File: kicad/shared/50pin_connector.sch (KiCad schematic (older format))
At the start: 1 part, among them P5 CONN_02X25

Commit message: connector
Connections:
- net /CS_RES02: now reaches P5.20 (P20)
- net /OE2: now reaches P5.37 (P37)
- net /WE2: now reaches P5.38 (P38)
- no-connect marks 0 -> 16

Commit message: connector
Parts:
- P5: footprint (none) -> Pin_Headers:Pin_Header_Angled_2x25
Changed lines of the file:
@@
 F 0 "P5" H 5550 5050 50  0000 C CNN
 F 1 "CONN_02X25" V 5550 3750 50  0000 C CNN
-F 2 "" H 5550 3000 60  0000 C CNN
+F 2 "Pin_Headers:Pin_Header_Angled_2x25" H 5550 3000 60  0001 C CNN
 F 3 "" H 5550 3000 60  0000 C CNN
 	1    5550 3750
@@
 Text Label 4850 2700 0    60   ~ 0
 D
-Text Label 4550 3750 0    60   ~ 0
+Text Label 4350 3750 0    60   ~ 0
 A[0..15]
-Text Label 6450 3650 0    60   ~ 0
-A
 Text GLabel 5250 4350 0    60   Input ~ 0
 /OE2
@@
 Text GLabel 5850 3450 2    60   Input ~ 0
 /CS_RES02
-Text HLabel 6650 3950 2    60   Input ~ 0
+Text HLabel 3550 4900 2    60   Input ~ 0
 A0
 Entry Wire Line
-	6450 3850 6550 3950
-Wire Wire Line
-	6550 3950 6650 3950
-Text HLabel 6650 3850 2    60   Input ~ 0
+	3350 4800 3450 4900
+Text HLabel 3550 4700 2    60   Input ~ 0
 A2
-Text HLabel 6650 3750 2    60   Input ~ 0
+Text HLabel 3550 4500 2    60   Input ~ 0
 A4
 Entry Wire Line
-	6450 3750 6550 3850
-Entry Wire Line
-	6450 3650 6550 3750
-Wire Wire Line
-	6550 3750 6650 3750
-Wire Wire Line
-	6650 3850 6550 3850
-Entry Wire Line
-	4550 3850 4650 3750
-Text HLabel 4550 3850 0    60   Input ~ 0
+	3350 4500 3450 4600
+Entry Wire Line
+	3350 4400 3450 4500
+Wire Wire Line
+	3450 4500 3550 4500
+Entry Wire Line
+	3450 4700 3350 4600
+Text HLabel 3550 4600 2    60   Input ~ 0
 A3
 Entry Wire Line
-	4550 3950 4650 3850
-Text HLabel 4550 3950 0    60   Input ~ 0
+	3450 4800 3350 4700
+Text HLabel 3550 4800 2    60   Input ~ 0
 A1
+Wire Bus Line
+	3350 4100 3350 4950
+Text Label 3350 4150 0    60   ~ 0
+A[0..15]
+Wire Wire Line
+	3450 4900 3550 4900
+Wire Wire Line
+	3450 4800 3550 4800
+Wire Wire Line
+	3450 4600 3550 4600
+Wire Wire Line
+	3550 4700 3450 4700
+Wire Bus Line
+	3350 2700 3350 3750
+Entry Wire Line
+	3350 3050 3450 3150
+Entry Wire Line
+	3350 3250 3450 3350
+Entry Wire Line
+	3350 3450 3450 3550
+Entry Wire Line
+	3350 3650 3450 3750
+Wire Wire Line
+	3450 3150 3600 3150
+Wire Wire Line
+	3450 3350 3600 3350
+Wire Wire Line
+	3450 3550 3600 3550
+Wire Wire Line
+	3450 3750 3600 3750
+Text Label 3450 3150 0    60   ~ 0
+D7
+Text Label 3450 3350 0    60   ~ 0
+D5
+Text Label 3450 3550 0    60   ~ 0
+D3
+Text Label 3450 3750 0    60   ~ 0
+D1
+Text Label 3350 2650 0    60   ~ 0
+D[0..7]
+Entry Wire Line
+	3450 3250 3350 3150
+Entry Wire Line
+	3450 3450 3350 3350
+Entry Wire Line
+	3450 3650 3350 3550
+Entry Wire Line
+	3450 3850 3350 3750
+Wire Wire Line
+	3600 3250 3450 3250
+Wire Wire Line
+	3600 3450 3450 3450
+Wire Wire Line
+	3600 3650 3450 3650
+Wire Wire Line
+	3600 3850 3450 3850
+Text Label 3550 3250 2    60   ~ 0
+D6
+Text Label 3550 3450 2    60   ~ 0
+D4
+Text Label 3550 3650 2    60   ~ 0
+D2
+Text Label 3550 3850 2    60   ~ 0
+D0
+Text HLabel 3600 3850 2    60   Input ~ 0
+D0
+Text HLabel 3600 3750 2    60   Input ~ 0
+D1
+Text HLabel 3600 3650 2    60   Input ~ 0
+D2
+Text HLabel 3600 3550 2    60   Input ~ 0
+D3
+Text HLabel 3600 3450 2    60   Input ~ 0
+D4
+Text HLabel 3600 3350 2    60   Input ~ 0
+D5
+Text HLabel 3600 3250 2    60   Input ~ 0
+D6
+Text HLabel 3600 3150 2    60   Input ~ 0
+D7
+Text Label 3450 4900 0    60   ~ 0
+A0
+Text Label 3450 4800 0    60   ~ 0
+A1
+Text Label 3450 4700 0    60   ~ 0
+A2
+Text Label 3450 4600 0    60   ~ 0
+A3
+Text Label 3450 4500 0    60   ~ 0
+A4
 $EndSCHEMATC

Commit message: connector
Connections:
- net /RW: now also P5.15 (P15); no longer P5.16 (P16)
- net D0: now also P5.13 (P13); no longer P5.14 (P14)
- net D1: now also P5.12 (P12); no longer P5.13 (P13)
- net D2: now also P5.11 (P11); no longer P5.12 (P12)
- net D3: now also P5.10 (P10); no longer P5.11 (P11)
- net D4: now also P5.9 (P9); no longer P5.10 (P10)
- net D5: now also P5.8 (P8); no longer P5.9 (P9)
- net D6: now also P5.7 (P7); no longer P5.8 (P8)
- net D7: now also P5.6 (P6); no longer P5.7 (P7)
- net GND: now also P5.47 (P47), P5.48 (P48), P5.49 (P49), P5.50 (P50)
- net RDY: now also P5.17 (P17); no longer P5.18 (P18)
- net VCC: now also P5.43 (P43), P5.44 (P44), P5.45 (P45), P5.46 (P46)
- net /CS_IO2: now reaches P5.19 (P19)
- net /ROMOFF: now reaches P5.5 (P5)
- net /CSR_VDP renamed /CS_VDP
- net /CSW_VDP renamed A5
- net /CS_RES02 renamed /CS_IO1
- net /CS_VIA renamed /CS_IO0
- net /OE2: no longer names the net of P5.37 (P37)
- net /WE2: no longer names the net of P5.38 (P38)
- net E_LCD renamed /CS_SND
- no-connect marks 16 -> 10
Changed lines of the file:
@@
 LIBS:contrib
 LIBS:valves
-LIBS:65xxx
-LIBS:gal
-LIBS:UART
-LIBS:osc
-LIBS:steckschwein-cache
 EELAYER 24 0
 EELAYER END
 $Descr A4 11693 8268
 encoding utf-8
-Sheet 2 2
+Sheet 1 1
 Title ""
 Date ""
@@
 /NMI
 Wire Bus Line
-	4850 2700 4850 3050
-Entry Wire Line
-	4850 2750 4950 2850
-Entry Wire Line
-	4850 2850 4950 2950
-Entry Wire Line
-	4850 2950 4950 3050
-Entry Wire Line
-	4850 3050 4950 3150
-Wire Wire Line
-	4950 2850 5300 2850
-Wire Wire Line
-	4950 2950 5300 2950
-Wire Wire Line
-	4950 3050 5300 3050
-Wire Wire Line
-	4950 3150 5300 3150
-Text Label 4950 2850 0    60   ~ 0
+	6400 2600 6400 2950
+Entry Wire Line
+	6400 2650 6300 2750
+Entry Wire Line
+	6400 2750 6300 2850
+Entry Wire Line
+	6400 2850 6300 2950
+Entry Wire Line
+	6400 2950 6300 3050
+Text Label 6300 2750 2    60   ~ 0
 D7
-Text Label 4950 2950 0    60   ~ 0
+Text Label 6300 2850 2    60   ~ 0
 D5
-Text Label 4950 3050 0    60   ~ 0
+Text Label 6300 2950 2    60   ~ 0
 D3
-Text Label 4950 3150 0    60   ~ 0
+Text Label 6300 3050 2    60   ~ 0
 D1
 Wire Bus Line
-	6300 2700 6300 3050
-Entry Wire Line
-	6200 2850 6300 2750
-Entry Wire Line
-	6200 2950 6300 2850
-Entry Wire Line
-	6200 3050 6300 2950
-Entry Wire Line
-	6200 3150 6300 3050
-Wire Wire Line
-	5800 2850 6200 2850
-Wire Wire Line
-	5800 2950 6200 2950
-Wire Wire Line
-	5800 3050 6200 3050
-Wire Wire Line
-	5800 3150 6200 3150
-Wire Wire Line
-	5800 3250 5850 3250
-Text GLabel 5850 3250 2    60   Input ~ 0
+	4650 2700 4650 3050
+Entry Wire Line
+	4750 2850 4650 2750
+Entry Wire Line
+	4750 2950 4650 2850
+Entry Wire Line
+	4750 3050 4650 2950
+Entry Wire Line
+	4750 3150 4650 3050
+Text GLabel 5250 3250 0    60   Input ~ 0
 /RW
-Text GLabel 5850 3350 2    60   Input ~ 0
+Text GLabel 5250 3350 0    60   Input ~ 0
 RDY
-Wire Wire Line
-	5800 3350 5850 3350
 Wire Wire Line
 	5300 3550 5250 3550
 Text GLabel 5250 3550 0    60   Input ~ 0
-E_LCD
+/CS_SND
 Wire Wire Line
 	5800 3550 5850 3550
 Text GLabel 5850 3550 2    60   Input ~ 0
-/CS_VIA
+/CS_IO0
 Text GLabel 5250 3650 0    60   Input ~ 0
 /CS_UART
@@
 	5300 3650 5250 3650
 Text GLabel 5850 3650 2    60   Input ~ 0
-/CSR_VDP
-Text GLabel 5250 3750 0    60   Input ~ 0
-/CSW_VDP
-Wire Wire Line
-	5250 3750 5300 3750
+/CS_VDP
+Wire Wire Line
+	4750 3750 5300 3750
 Wire Wire Line
 	5800 3650 5850 3650
@@
 	5800 3950 6350 3950
 Wire Bus Line
-	4650 3750 4650 4000
+	4650 3650 4650 4000
 Entry Wire Line
 	4650 3750 4750 3850
@@
 Text GLabel 5850 4150 2    60   Input ~ 0
 /WE
-Text Label 6100 2850 0    60   ~ 0
+Text Label 4850 2850 2    60   ~ 0
 D6
-Text Label 6100 2950 0    60   ~ 0
+Text Label 4850 2950 2    60   ~ 0
 D4
-Text Label 6100 3050 0    60   ~ 0
+Text Label 4850 3050 2    60   ~ 0
 D2
-Text Label 6100 3150 0    60   ~ 0
+Text Label 4850 3150 2    60   ~ 0
 D0
 Text Label 6250 3950 0    60   ~ 0
@@
 Text Label 4750 3850 0    60   ~ 0
 A3
-Text Label 6300 2700 0    60   ~ 0
+Text Label 4850 2700 2    60   ~ 0
 D
-Text Label 4850 2700 0    60   ~ 0
+Text Label 6400 2600 2    60   ~ 0
 D
-Text Label 4350 3750 0    60   ~ 0
+Text Label 4300 3650 0    60   ~ 0
 A[0..15]
-Text GLabel 5250 4350 0    60   Input ~ 0
-/OE2
-Text GLabel 5850 4350 2    60   Input ~ 0
-/WE2
-Wire Wire Line
-	5850 4350 5800 4350
-Wire Wire Line
-	5250 4350 5300 4350
-NoConn ~ 5300 3250
-NoConn ~ 5300 3350
-NoConn ~ 5300 3450
 NoConn ~ 5800 4250
 NoConn ~ 5300 4450
 NoConn ~ 5300 4550
-NoConn ~ 5300 4650
-NoConn ~ 5300 4750
-NoConn ~ 5300 4850
-NoConn ~ 5300 4950
 NoConn ~ 5800 4450
 NoConn ~ 5800 4550
-NoConn ~ 5800 4650
-NoConn ~ 5800 4750
-NoConn ~ 5800 4850
-NoConn ~ 5800 4950
 Wire Wire Line
 	5800 3450 5850 3450
 Text GLabel 5850 3450 2    60   Input ~ 0
-/CS_RES02
+/CS_IO1
 Text HLabel 3550 4900 2    60   Input ~ 0
 A0
@@
 Text Label 3450 4500 0    60   ~ 0
 A4
+Text GLabel 5250 3450 0    60   Input ~ 0
+/CS_IO2
+Wire Wire Line
+	5250 3450 5300 3450
+Wire Wire Line
+	5250 3350 5300 3350
+NoConn ~ 5800 3350
+Wire Wire Line
+	5300 2850 4750 2850
+Wire Wire Line
+	5300 2950 4750 2950
+Wire Wire Line
+	5300 3050 4750 3050
+Wire Wire Line
+	5300 3150 4750 3150
+Wire Wire Line
+	5800 2750 6300 2750
+Wire Wire Line
+	6300 2850 5800 2850
+Wire Wire Line
+	6300 2950 5800 2950
+Wire Wire Line
+	6300 3050 5800 3050
+Text GLabel 5250 2750 0    60   Input ~ 0
+/ROMOFF
+Wire Wire Line
+	5250 2750 5300 2750
+NoConn ~ 5800 3150
+Wire Wire Line
+	5250 3250 5300 3250
+NoConn ~ 5800 3250
+Entry Wire Line
+	4650 3650 4750 3750
+Text Label 4750 3750 0    60   ~ 0
+A5
+NoConn ~ 5800 4350
+NoConn ~ 5300 4350
+$Comp
+L GND #PWR?
+U 1 1 5436D639
+P 5250 5150
+F 0 "#PWR?" H 5250 5150 30  0001 C CNN
+F 1 "GND" H 5250 5080 30  0001 C CNN
+F 2 "" H 5250 5150 60  0000 C CNN
+F 3 "" H 5250 5150 60  0000 C CNN
+	1    5250 5150
+	1    0    0    -1
+$EndComp
+Wire Wire Line
+	5300 4850 5250 4850
+Wire Wire Line
+	5250 4850 5250 5150
+Wire Wire Line
+	5300 4950 5250 4950
+Connection ~ 5250 4950
+$Comp
+L VCC #PWR?
+U 1 1 5436D6BC
+P 5950 4550
+F 0 "#PWR?" H 5950 4650 30  0001 C CNN
+F 1 "VCC" H 5950 4650 30  0000 C CNN
+F 2 "" H 5950 4550 60  0000 C CNN
+F 3 "" H 5950 4550 60  0000 C CNN
+	1    5950 4550
+	1    0    0    -1
+$EndComp
+Wire Wire Line
+	5800 4850 5900 4850
+Wire Wire Line
+	5900 4850 5900 5050
+Wire Wire Line
+	5900 5050 5250 5050
+Connection ~ 5250 5050
+Wire Wire Line
+	5800 4950 5900 4950
+Connection ~ 5900 4950
+Wire Wire Line
+	5800 4650 5950 4650
+Wire Wire Line
+	5950 4550 5950 4750
+Wire Wire Line
+	5950 4750 5800 4750
+Connection ~ 5950 4650
+$Comp
+L VCC #PWR?
+U 1 1 5436D806
+P 5150 4550
+F 0 "#PWR?" H 5150 4650 30  0001 C CNN
+F 1 "VCC" H 5150 4650 30  0000 C CNN
+F 2 "" H 5150 4550 60  0000 C CNN
+F 3 "" H 5150 4550 60  0000 C CNN
+	1    5150 4550
+	1    0    0    -1
+$EndComp
+Wire Wire Line
+	5150 4550 5150 4750
+Wire Wire Line
+	5150 4750 5300 4750
+Wire Wire Line
+	5300 4650 5150 4650
+Connection ~ 5150 4650
 $EndSCHEMATC

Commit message: connector A5
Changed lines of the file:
@@
 LIBS:contrib
 LIBS:valves
+LIBS:50pin_connector-cache
 EELAYER 24 0
 EELAYER END
@@
 	5300 4650 5150 4650
 Connection ~ 5150 4650
+Entry Wire Line
+	3350 4300 3450 4400
+Text HLabel 3550 4400 2    60   Input ~ 0
+A5
+Wire Wire Line
+	3450 4400 3550 4400
+Text Label 3450 4400 0    60   ~ 0
+A5
 $EndSCHEMATC

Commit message: update
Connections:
- net /CS_IO2 is gone; now on net /CS_IO1: P5.19 (P19)
- net /CS_IO0: now also P5.20 (P20); no longer P5.22 (P22)
- net /CS_IO1: no longer P5.20 (P20)
- new net /CS_VIA: P5.22 (P22)
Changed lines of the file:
@@
 LIBS:contrib
 LIBS:valves
-LIBS:50pin_connector-cache
+LIBS:65xxx
+LIBS:gal
+LIBS:UART
+LIBS:osc
+LIBS:74xgxx
+LIBS:ttl_ieee
+LIBS:steckschwein-cache
 EELAYER 24 0
 EELAYER END
 $Descr A4 11693 8268
 encoding utf-8
-Sheet 1 1
+Sheet 2 2
 Title ""
 Date ""
@@
 $EndComp
 $Comp
-L VCC #PWR019
+L VCC #PWR028
 U 1 1 54207202
 P 5200 2400
-F 0 "#PWR019" H 5200 2500 30  0001 C CNN
+F 0 "#PWR028" H 5200 2500 30  0001 C CNN
 F 1 "VCC" H 5200 2500 30  0000 C CNN
 F 2 "" H 5200 2400 60  0000 C CNN
@@
 Wire Wire Line
 	5800 3550 5850 3550
-Text GLabel 5850 3550 2    60   Input ~ 0
+Text GLabel 5850 3450 2    60   Input ~ 0
 /CS_IO0
 Text GLabel 5250 3650 0    60   Input ~ 0
@@
 	4750 3950 5300 3950
 $Comp
-L GND #PWR020
+L GND #PWR029
 U 1 1 54207240
 P 4700 4100
-F 0 "#PWR020" H 4700 4100 30  0001 C CNN
+F 0 "#PWR029" H 4700 4100 30  0001 C CNN
 F 1 "GND" H 4700 4030 30  0001 C CNN
 F 2 "" H 4700 4100 60  0000 C CNN
@@
 	4700 4050 5300 4050
 $Comp
-L GND #PWR021
+L GND #PWR030
 U 1 1 54207248
 P 6350 4100
-F 0 "#PWR021" H 6350 4100 30  0001 C CNN
+F 0 "#PWR030" H 6350 4100 30  0001 C CNN
 F 1 "GND" H 6350 4030 30  0001 C CNN
 F 2 "" H 6350 4100 60  0000 C CNN
@@
 Wire Wire Line
 	5800 3450 5850 3450
-Text GLabel 5850 3450 2    60   Input ~ 0
+Text GLabel 5250 3450 0    60   Input ~ 0
 /CS_IO1
 Text HLabel 3550 4900 2    60   Input ~ 0
@@
 Text Label 3450 4500 0    60   ~ 0
 A4
-Text GLabel 5250 3450 0    60   Input ~ 0
-/CS_IO2
 Wire Wire Line
 	5250 3450 5300 3450
@@
 NoConn ~ 5300 4350
 $Comp
-L GND #PWR?
+L GND #PWR031
 U 1 1 5436D639
 P 5250 5150
-F 0 "#PWR?" H 5250 5150 30  0001 C CNN
+F 0 "#PWR031" H 5250 5150 30  0001 C CNN
 F 1 "GND" H 5250 5080 30  0001 C CNN
 F 2 "" H 5250 5150 60  0000 C CNN
@@
 Connection ~ 5250 4950
 $Comp
-L VCC #PWR?
+L VCC #PWR032
 U 1 1 5436D6BC
 P 5950 4550
-F 0 "#PWR?" H 5950 4650 30  0001 C CNN
+F 0 "#PWR032" H 5950 4650 30  0001 C CNN
 F 1 "VCC" H 5950 4650 30  0000 C CNN
 F 2 "" H 5950 4550 60  0000 C CNN
@@
 Connection ~ 5950 4650
 $Comp
-L VCC #PWR?
+L VCC #PWR033
 U 1 1 5436D806
 P 5150 4550
-F 0 "#PWR?" H 5150 4650 30  0001 C CNN
+F 0 "#PWR033" H 5150 4650 30  0001 C CNN
 F 1 "VCC" H 5150 4650 30  0000 C CNN
 F 2 "" H 5150 4550 60  0000 C CNN
@@
 Text Label 3450 4400 0    60   ~ 0
 A5
+Text GLabel 5850 3550 2    60   Input ~ 0
+/CS_VIA
 $EndSCHEMATC

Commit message: connector
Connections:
- net /CS_SND is gone; now on net /CS_IO0: P5.21 (P21)
- net /CS_IO0: no longer P5.20 (P20)
- net /CS_IO1: now also P5.20 (P20); no longer P5.19 (P19)
- net /ROMOFF: no longer names the net of P5.5 (P5)
- new net /CS_IO2: P5.19 (P19)
- no-connect marks 10 -> 11
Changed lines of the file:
@@
 $Descr A4 11693 8268
 encoding utf-8
-Sheet 2 2
+Sheet 2 3
 Title ""
 Date ""
@@
 $EndComp
 $Comp
-L VCC #PWR028
+L VCC #PWR022
 U 1 1 54207202
 P 5200 2400
-F 0 "#PWR028" H 5200 2500 30  0001 C CNN
+F 0 "#PWR022" H 5200 2500 30  0001 C CNN
 F 1 "VCC" H 5200 2500 30  0000 C CNN
 F 2 "" H 5200 2400 60  0000 C CNN
@@
 	5300 3550 5250 3550
 Text GLabel 5250 3550 0    60   Input ~ 0
-/CS_SND
+/CS_IO0
 Wire Wire Line
 	5800 3550 5850 3550
 Text GLabel 5850 3450 2    60   Input ~ 0
-/CS_IO0
+/CS_IO1
 Text GLabel 5250 3650 0    60   Input ~ 0
 /CS_UART
@@
 	4750 3950 5300 3950
 $Comp
-L GND #PWR029
+L GND #PWR023
 U 1 1 54207240
 P 4700 4100
-F 0 "#PWR029" H 4700 4100 30  0001 C CNN
+F 0 "#PWR023" H 4700 4100 30  0001 C CNN
 F 1 "GND" H 4700 4030 30  0001 C CNN
 F 2 "" H 4700 4100 60  0000 C CNN
@@
 	4700 4050 5300 4050
 $Comp
-L GND #PWR030
+L GND #PWR024
 U 1 1 54207248
 P 6350 4100
-F 0 "#PWR030" H 6350 4100 30  0001 C CNN
+F 0 "#PWR024" H 6350 4100 30  0001 C CNN
 F 1 "GND" H 6350 4030 30  0001 C CNN
 F 2 "" H 6350 4100 60  0000 C CNN
@@
 	5800 3450 5850 3450
 Text GLabel 5250 3450 0    60   Input ~ 0
-/CS_IO1
+/CS_IO2
 Text HLabel 3550 4900 2    60   Input ~ 0
 A0
@@
 Wire Wire Line
 	6300 3050 5800 3050
-Text GLabel 5250 2750 0    60   Input ~ 0
-/ROMOFF
-Wire Wire Line
-	5250 2750 5300 2750
 NoConn ~ 5800 3150
 Wire Wire Line
@@
 NoConn ~ 5300 4350
 $Comp
-L GND #PWR031
+L GND #PWR025
 U 1 1 5436D639
 P 5250 5150
-F 0 "#PWR031" H 5250 5150 30  0001 C CNN
+F 0 "#PWR025" H 5250 5150 30  0001 C CNN
 F 1 "GND" H 5250 5080 30  0001 C CNN
 F 2 "" H 5250 5150 60  0000 C CNN
@@
 Connection ~ 5250 4950
 $Comp
-L VCC #PWR032
+L VCC #PWR026
 U 1 1 5436D6BC
 P 5950 4550
-F 0 "#PWR032" H 5950 4650 30  0001 C CNN
+F 0 "#PWR026" H 5950 4650 30  0001 C CNN
 F 1 "VCC" H 5950 4650 30  0000 C CNN
 F 2 "" H 5950 4550 60  0000 C CNN
@@
 Connection ~ 5950 4650
 $Comp
-L VCC #PWR033
+L VCC #PWR027
 U 1 1 5436D806
 P 5150 4550
-F 0 "#PWR033" H 5150 4650 30  0001 C CNN
+F 0 "#PWR027" H 5150 4650 30  0001 C CNN
 F 1 "VCC" H 5150 4650 30  0000 C CNN
 F 2 "" H 5150 4550 60  0000 C CNN
@@
 Text GLabel 5850 3550 2    60   Input ~ 0
 /CS_VIA
+NoConn ~ 5300 2750
 $EndSCHEMATC

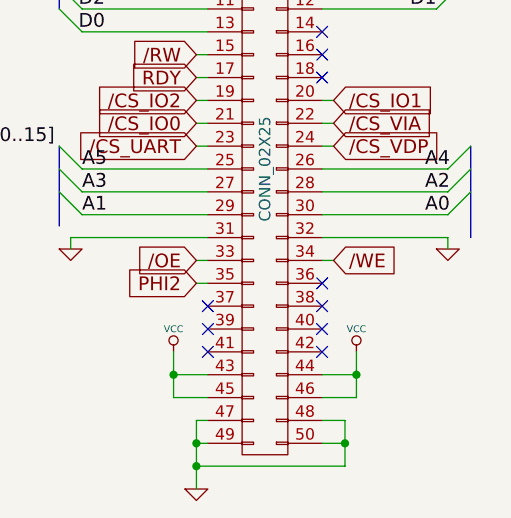
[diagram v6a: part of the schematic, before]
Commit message: RESET_TRIG pin
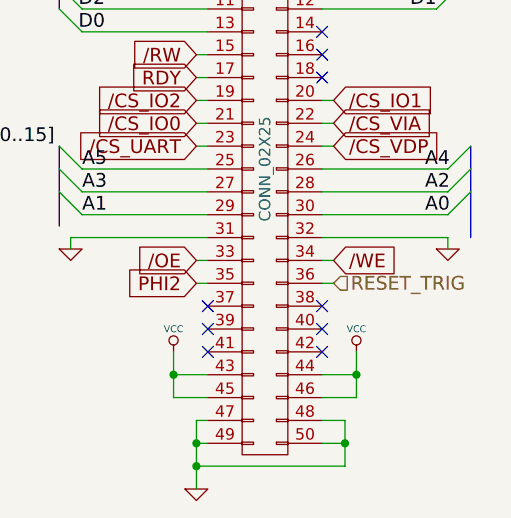
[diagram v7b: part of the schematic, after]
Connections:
- net RESET_TRIG: now reaches P5.36 (P36)
- no-connect marks 11 -> 10
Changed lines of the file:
@@
 LIBS:ttl_ieee
 LIBS:steckschwein-cache
-EELAYER 24 0
+EELAYER 25 0
 EELAYER END
 $Descr A4 11693 8268
@@
 $EndComp
 $Comp
-L VCC #PWR022
+L VCC #PWR023
 U 1 1 54207202
 P 5200 2400
-F 0 "#PWR022" H 5200 2500 30  0001 C CNN
+F 0 "#PWR023" H 5200 2500 30  0001 C CNN
 F 1 "VCC" H 5200 2500 30  0000 C CNN
 F 2 "" H 5200 2400 60  0000 C CNN
@@
 	4750 3950 5300 3950
 $Comp
-L GND #PWR023
+L GND #PWR024
 U 1 1 54207240
 P 4700 4100
-F 0 "#PWR023" H 4700 4100 30  0001 C CNN
+F 0 "#PWR024" H 4700 4100 30  0001 C CNN
 F 1 "GND" H 4700 4030 30  0001 C CNN
 F 2 "" H 4700 4100 60  0000 C CNN
@@
 	4700 4050 5300 4050
 $Comp
-L GND #PWR024
+L GND #PWR025
 U 1 1 54207248
 P 6350 4100
-F 0 "#PWR024" H 6350 4100 30  0001 C CNN
+F 0 "#PWR025" H 6350 4100 30  0001 C CNN
 F 1 "GND" H 6350 4030 30  0001 C CNN
 F 2 "" H 6350 4100 60  0000 C CNN
@@
 Text Label 4300 3650 0    60   ~ 0
 A[0..15]
-NoConn ~ 5800 4250
 NoConn ~ 5300 4450
 NoConn ~ 5300 4550
@@
 NoConn ~ 5300 4350
 $Comp
-L GND #PWR025
+L GND #PWR026
 U 1 1 5436D639
 P 5250 5150
-F 0 "#PWR025" H 5250 5150 30  0001 C CNN
+F 0 "#PWR026" H 5250 5150 30  0001 C CNN
 F 1 "GND" H 5250 5080 30  0001 C CNN
 F 2 "" H 5250 5150 60  0000 C CNN
@@
 Connection ~ 5250 4950
 $Comp
-L VCC #PWR026
+L VCC #PWR027
 U 1 1 5436D6BC
 P 5950 4550
-F 0 "#PWR026" H 5950 4650 30  0001 C CNN
+F 0 "#PWR027" H 5950 4650 30  0001 C CNN
 F 1 "VCC" H 5950 4650 30  0000 C CNN
 F 2 "" H 5950 4550 60  0000 C CNN
@@
 Connection ~ 5950 4650
 $Comp
-L VCC #PWR027
+L VCC #PWR028
 U 1 1 5436D806
 P 5150 4550
-F 0 "#PWR027" H 5150 4650 30  0001 C CNN
+F 0 "#PWR028" H 5150 4650 30  0001 C CNN
 F 1 "VCC" H 5150 4650 30  0000 C CNN
 F 2 "" H 5150 4550 60  0000 C CNN
@@
 /CS_VIA
 NoConn ~ 5300 2750
+Text HLabel 5850 4250 2    60   Input ~ 0
+RESET_TRIG
+Wire Wire Line
+	5800 4250 5850 4250
 $EndSCHEMATC

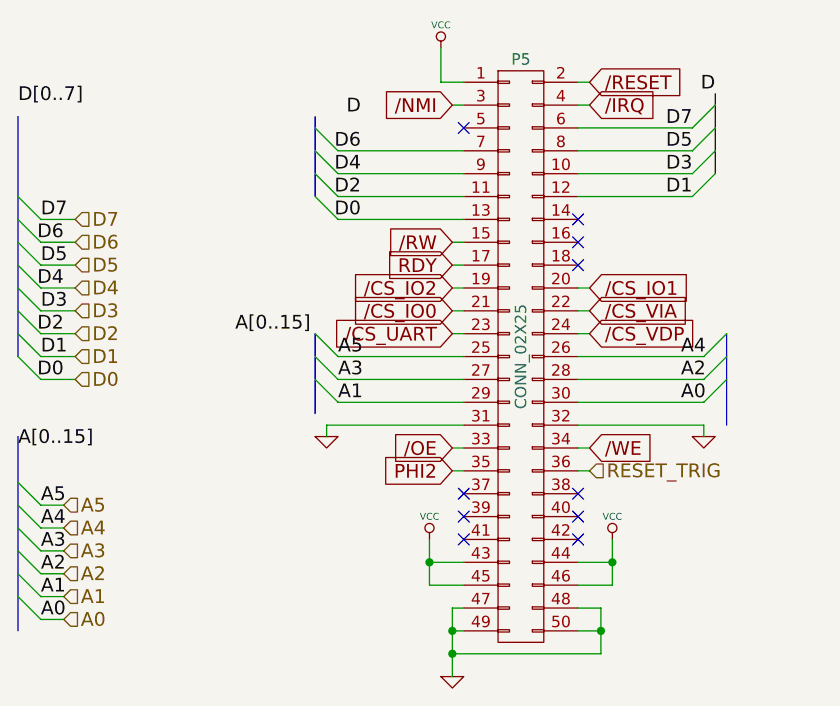
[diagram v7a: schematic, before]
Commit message: phi2 flankiert von gnd
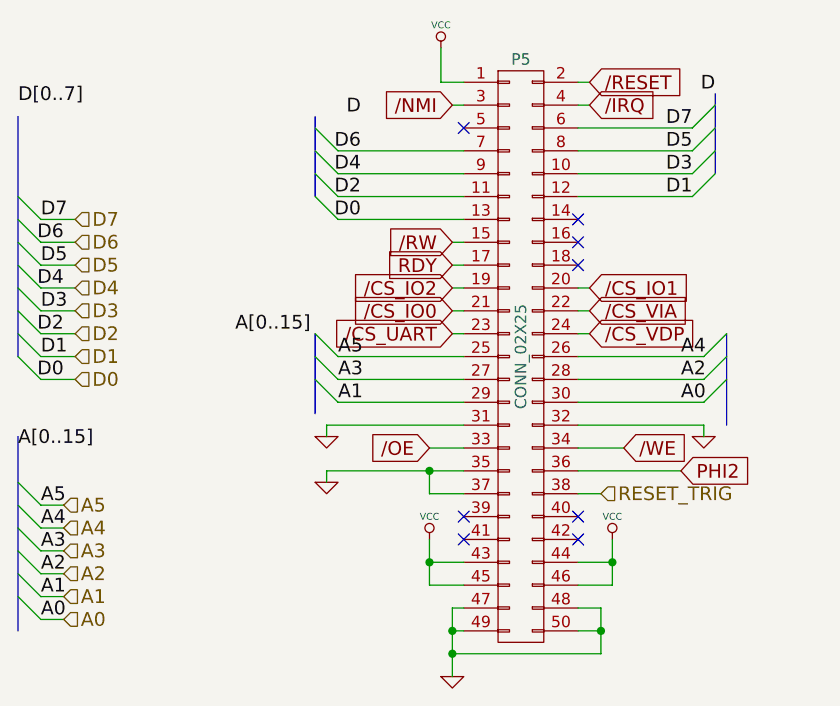
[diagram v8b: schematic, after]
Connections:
- net GND: now also P5.35 (P35), P5.37 (P37)
- net PHI2: now also P5.36 (P36); no longer P5.35 (P35)
- net RESET_TRIG: now also P5.38 (P38); no longer P5.36 (P36)
- no-connect marks 10 -> 8
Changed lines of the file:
@@
 	6350 4050 6350 4100
 Wire Wire Line
-	5300 4150 5250 4150
-Wire Wire Line
-	5300 4250 5250 4250
-Wire Wire Line
-	5800 4150 5850 4150
-Text GLabel 5250 4150 0    60   Input ~ 0
+	5300 4150 5150 4150
+Wire Wire Line
+	5800 4150 6000 4150
+Text GLabel 5150 4150 0    60   Input ~ 0
 /OE
-Text GLabel 5250 4250 0    60   Input ~ 0
+Text GLabel 6250 4250 2    60   Input ~ 0
 PHI2
-Text GLabel 5850 4150 2    60   Input ~ 0
+Text GLabel 6000 4150 2    60   Input ~ 0
 /WE
 Text Label 4850 2850 2    60   ~ 0
@@
 Text Label 4750 3750 0    60   ~ 0
 A5
-NoConn ~ 5800 4350
-NoConn ~ 5300 4350
 $Comp
 L GND #PWR026
@@
 /CS_VIA
 NoConn ~ 5300 2750
-Text HLabel 5850 4250 2    60   Input ~ 0
+Text HLabel 5900 4350 2    60   Input ~ 0
 RESET_TRIG
-Wire Wire Line
-	5800 4250 5850 4250
+$Comp
+L GND #PWR?
+U 1 1 54BC2AE5
+P 4700 4300
+F 0 "#PWR?" H 4700 4300 30  0001 C CNN
+F 1 "GND" H 4700 4230 30  0001 C CNN
+F 2 "" H 4700 4300 60  0000 C CNN
+F 3 "" H 4700 4300 60  0000 C CNN
+	1    4700 4300
+	1    0    0    -1
+$EndComp
+Wire Wire Line
+	4700 4300 4700 4250
+Wire Wire Line
+	4700 4250 5300 4250
+Wire Wire Line
+	5800 4250 6250 4250
+Wire Wire Line
+	5300 4350 5150 4350
+Wire Wire Line
+	5150 4350 5150 4250
+Connection ~ 5150 4250
+Wire Wire Line
+	5800 4350 5900 4350
 $EndSCHEMATC
